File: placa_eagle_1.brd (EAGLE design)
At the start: 88.2 x 35.5 mm, 19 parts, among them J1 CONN_0227-2021, J2 CONN_0427-2041, J3 CONN_0227-2021, J4 CONN_0227-2021, J5 CONN_0427-2041

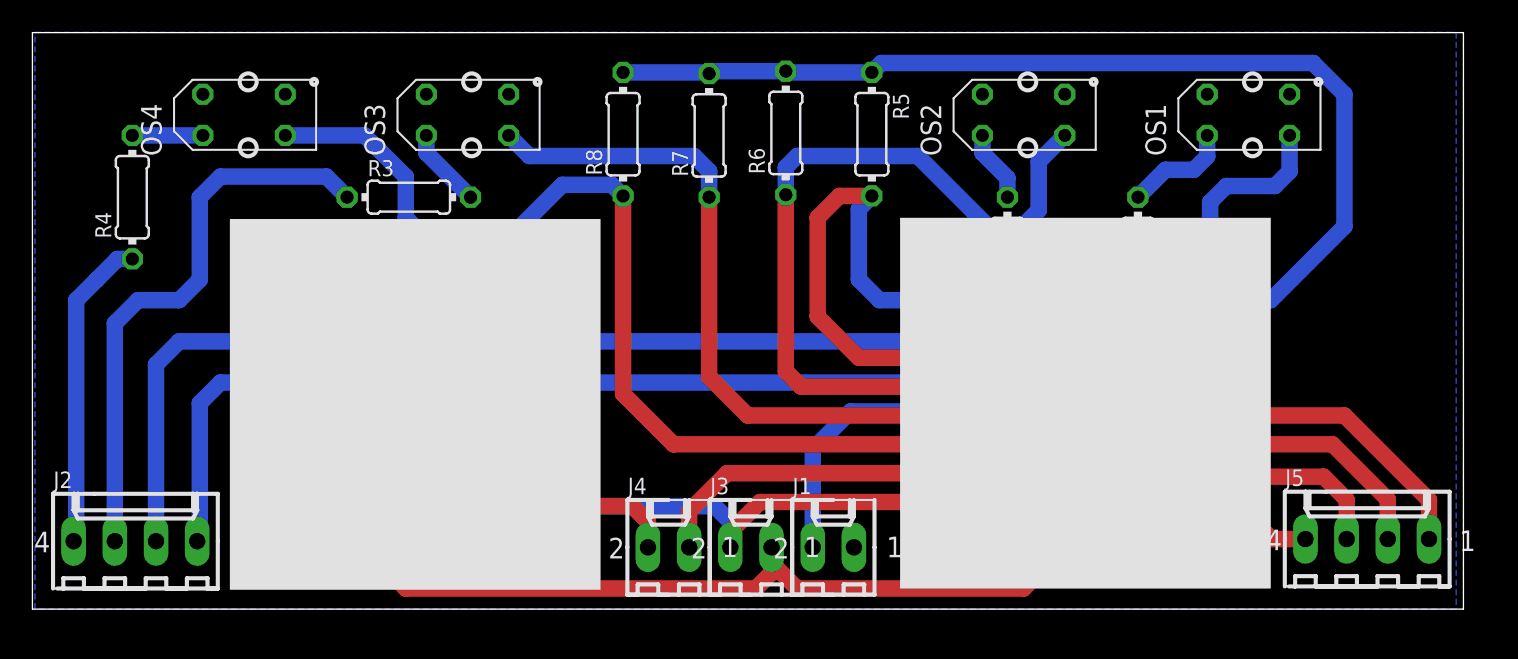
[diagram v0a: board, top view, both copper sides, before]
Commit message: praca china:
foi ajustado a posição dos conectores.
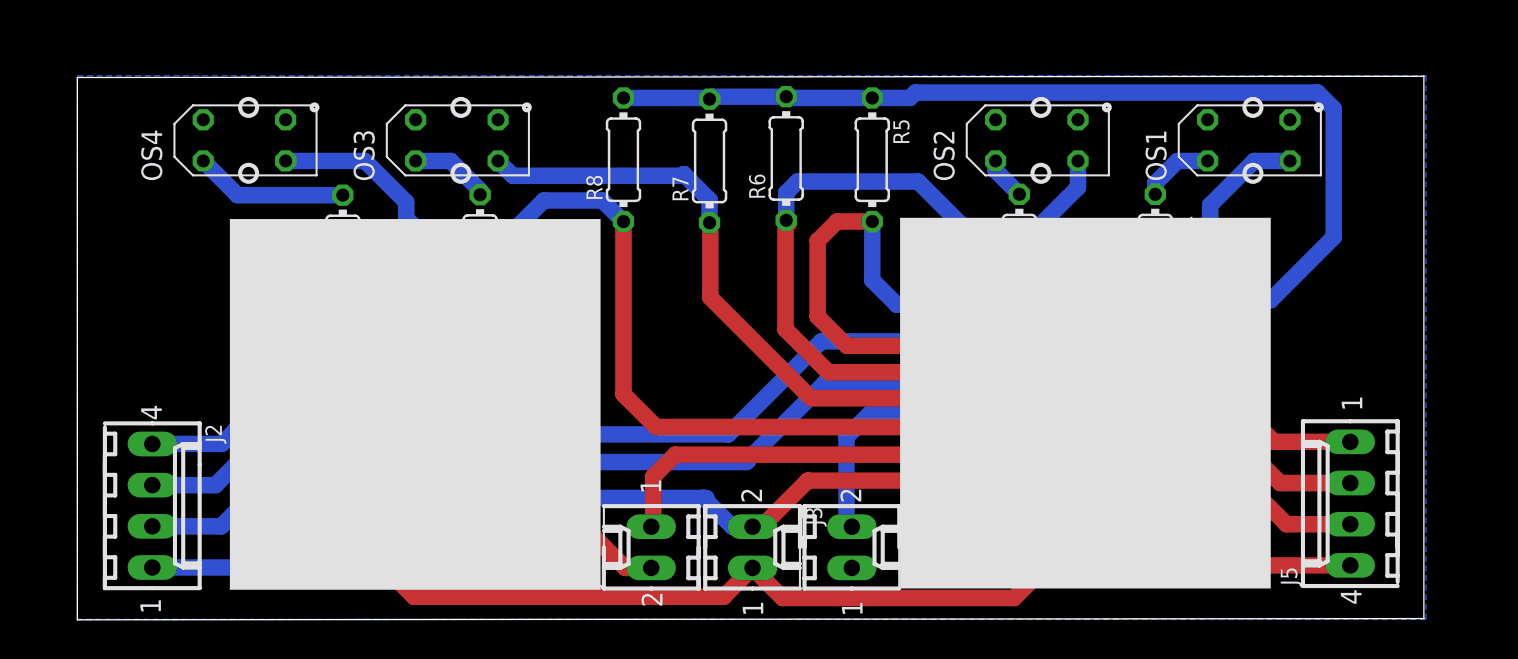
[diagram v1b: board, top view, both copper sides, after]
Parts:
- moved R4 13.5 mm to (21.5, 63.6)
- moved R3 5.72 mm to (30.0, 63.7), turned to 90 degrees
- moved J5 2.42 mm to (83.6, 48.4), turned to 90 degrees
- moved J2 2.42 mm to (9.77, 48.3), turned to 270 degrees
- moved OS2 1.77 mm to (64.3, 70.8)
- moved OS3 1.71 mm to (28.5, 70.8)
- moved R5 1.58 mm to (54.2, 69.6)
- moved R6 1.58 mm to (48.9, 69.7)
- moved R7 1.58 mm to (44.1, 69.5)
- moved R8 1.58 mm to (38.8, 69.6)
- moved OS1 1.58 mm to (77.4, 70.8)
- moved OS4 1.58 mm to (15.5, 70.8)
- moved J1 1.14 mm to (52.9, 45.7), turned to 270 degrees
- moved R1 1.08 mm to (71.6, 63.7)
- moved J4 1.07 mm to (40.5, 45.7), turned to 90 degrees
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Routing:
- net N$5: track 94.6 -> 79.8 mm
- net N$6: track 78.9 -> 69.6 mm
- net N$11: track 35.2 -> 26.8 mm
- net N$10: track 64.7 -> 58.8 mm
- net N$7: track 70.8 -> 65.4 mm
- net N$4: track 4.35 -> 9.48 mm
- net VCC: track 98.4 -> 93.3 mm
- net N$14: track 32.8 -> 36.2 mm
- net N$1: track 6.61 -> 4.48 mm
- net N$2: track 4.45 -> 2.66 mm
- net N$12: track 19.4 -> 18.3 mm
- net N$8: track 84.6 -> 85.8 mm
- net N$18: track 48.4 -> 47.5 mm
- net N$16: track 47.1 -> 46.4 mm
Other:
- board size 88.2 x 35.5 mm -> 83 x 33.5 mm
